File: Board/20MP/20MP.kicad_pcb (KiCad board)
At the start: 2 copper layers, 103.2 x 100 mm, 49 parts, among them J1 Conn_01x02_Male, SW1 SHOU_HAN_MSK12C02-HB, SW2 RotaryEncoder_Switch, U1 nice_nanoV2

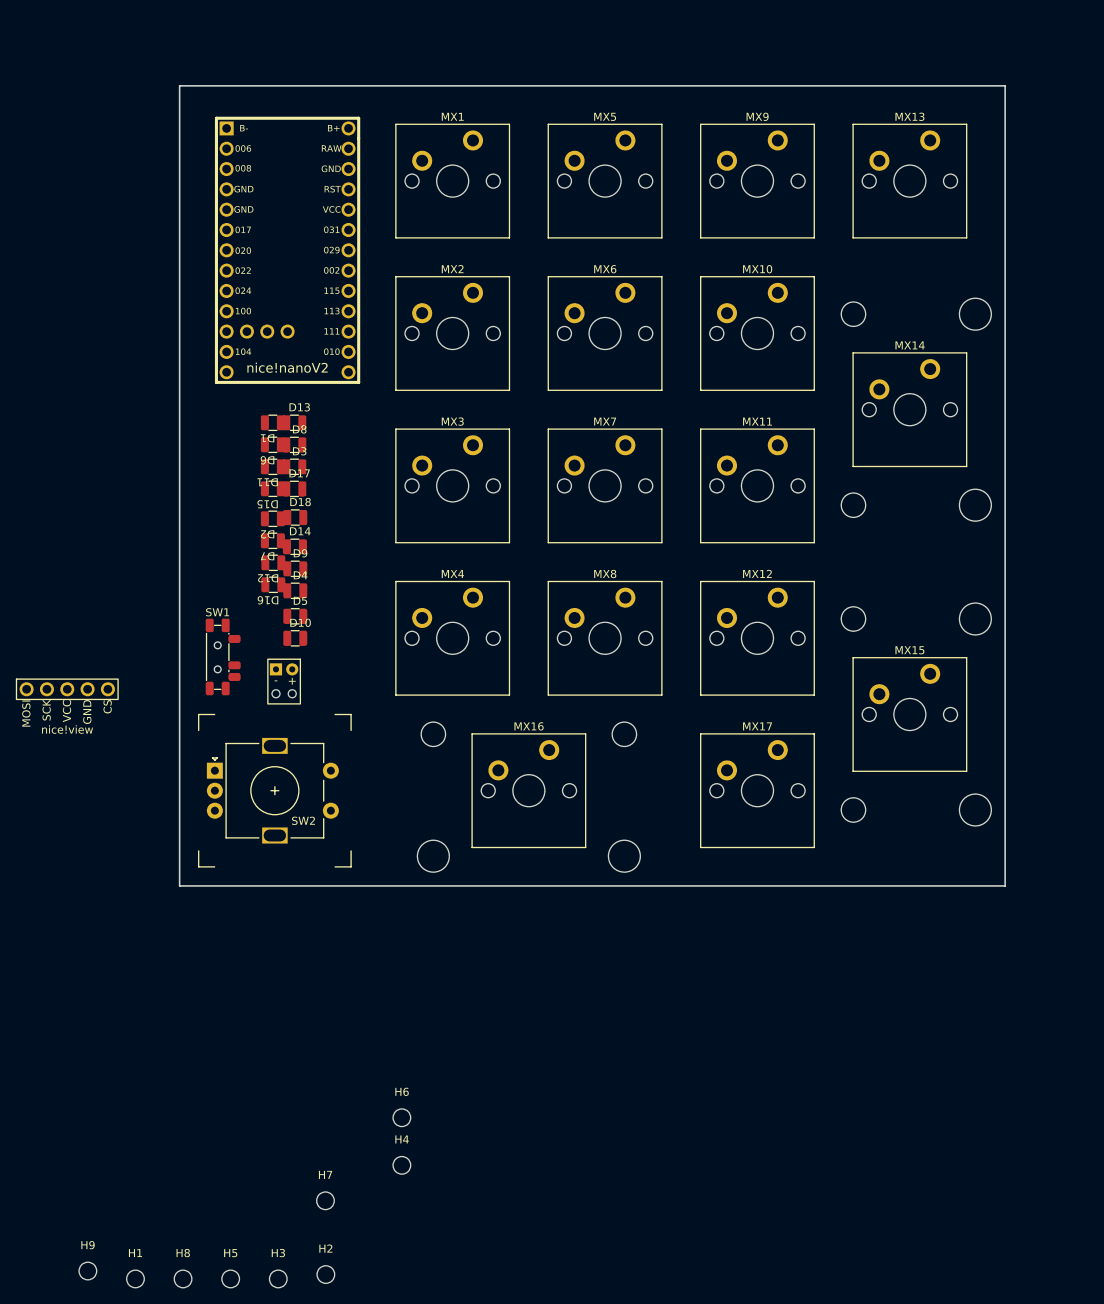
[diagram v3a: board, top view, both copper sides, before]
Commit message: added matrix traces
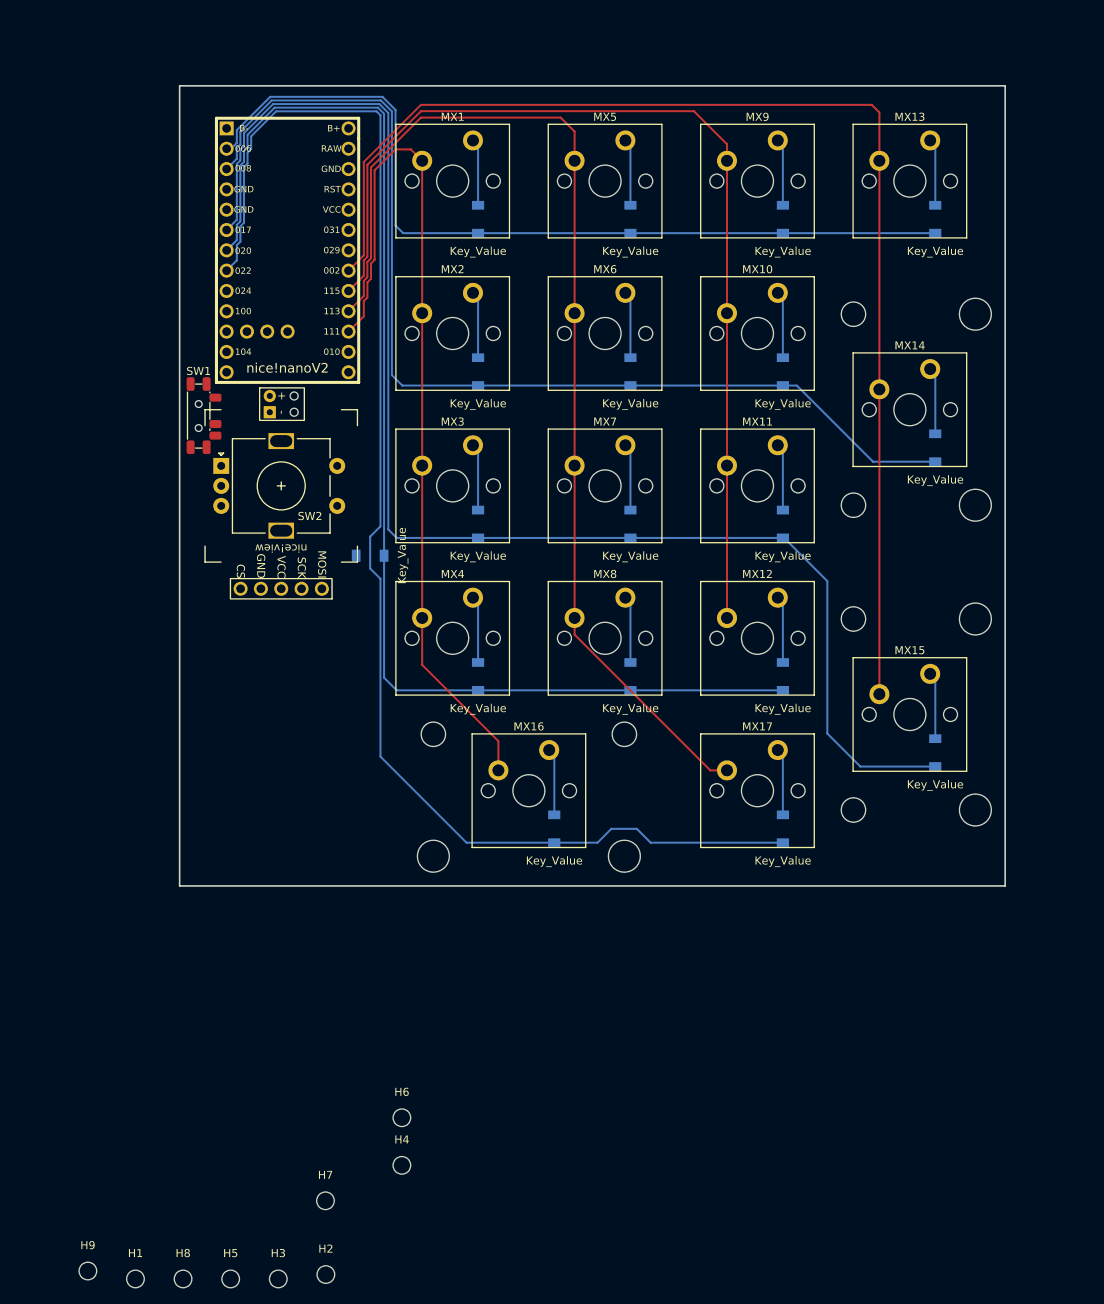
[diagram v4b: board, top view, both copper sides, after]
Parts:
- D1, D10, D11, D12, D13, D14, D15, D16, D17, D18, D2, D3, D4, D5, D6, D7, D8, D9: footprint led:led_capacitor -> led:D_SOD-123; moved to B.Cu
- U1: value nice_nanoV2 -> nice_nano
- moved D15 89.4 mm to (146.1, 50.8), turned to 90 degrees
- moved D17 86.6 mm to (146.1, 117.5), turned to 90 degrees
- moved D16 84.5 mm to (146.1, 79.4), turned to 90 degrees
- moved D11 70.9 mm to (127.0, 50.8), turned to 90 degrees
- moved D12 68.0 mm to (127.0, 69.8), turned to 90 degrees
- moved D10 65.4 mm to (127.0, 127.0), turned to 90 degrees
- moved D14 63.1 mm to (127.0, 108.0), turned to 90 degrees
- moved D13 62.4 mm to (127.0, 88.9), turned to 90 degrees
- moved D6 52.9 mm to (108.0, 50.8), turned to 90 degrees
- moved D7 49.5 mm to (108.0, 69.8), turned to 90 degrees
- moved D9 44.0 mm to (108.0, 108.0), turned to 90 degrees
- moved D8 43.2 mm to (108.0, 88.9), turned to 90 degrees
- moved D5 41.9 mm to (98.4, 127.0), turned to 90 degrees
- moved SW2 38.1 mm to (64.3, 84.1)
- moved D1 36.1 mm to (88.9, 50.8), turned to 90 degrees
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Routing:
- net ROW2: track 0.00 -> 176.9 mm
- net ROW4: track 0.00 -> 173.2 mm
- net ROW3: track 0.00 -> 155.3 mm
- net COL3: track 0.00 -> 154.9 mm
- net COL1: track 0.00 -> 136.9 mm
- net ROW1: track 0.00 -> 131.9 mm
- net COL2: track 0.00 -> 125.4 mm
- net COL0: track 0.00 -> 109.3 mm
- net ROW0: track 0.00 -> 107.7 mm
- net Net-(D17-Pad2): track 0.00 -> 8.36 mm
- net Net-(D16-Pad2): track 0.00 -> 8.36 mm
- net Net-(D15-Pad2): track 0.00 -> 8.36 mm
- net Net-(D10-Pad2): track 0.00 -> 8.36 mm
- net Net-(D7-Pad2): track 0.00 -> 8.36 mm
- net Net-(D6-Pad2): track 0.00 -> 8.36 mm
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
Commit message: added power
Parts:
- moved J1 5.43 mm to (65.4, 75.8), turned to 90 degrees
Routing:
- net B+: track 0.00 -> 57.4 mm, vias 0 -> 2
- net B-: track 0.00 -> 38.1 mm
- net COL3: track 154.9 -> 179.9 mm
- net Net-(J1-Pad2): track 0.00 -> 9.35 mm
- net Net-(D18-Pad2): track 0.00 -> 7.21 mm
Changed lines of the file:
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@@
   )
   (footprint "led:THT_Battery" (layer "F.Cu")
-    (at 61.59475 71.88175 -90)
+    (at 65.40525 75.75575 90)
     (property "Sheetfile" "20MP.kicad_sch")
     (property "Sheetname" "")
     (attr through_hole)
-    (fp_text reference "J1" (at 2.032 -6.604 -90 unlocked) (layer "F.SilkS") hide
-      (effects (font (size 1 1) (thickness 0.15)))
-    )
-    (fp_text value "Conn_01x02_Male" (at 2.187 -6.699 -90 unlocked) (layer "F.Fab")
-      (effects (font (size 1 1) (thickness 0.15)))
-    )
-    (fp_text user "-" (at 3.048 -2.794 -90 unlocked) (layer "F.SilkS")
-      (effects (font (size 1 1) (thickness 0.15)))
-    )
-    (fp_text user "+" (at 1.016 -2.794 -90 unlocked) (layer "F.SilkS")
+    (fp_text reference "J1" (at 2.032 -6.604 90 unlocked) (layer "F.SilkS") hide
+      (effects (font (size 1 1) (thickness 0.15)))
+    )
+    (fp_text value "Conn_01x02_Male" (at 2.187 -6.699 90 unlocked) (layer "F.Fab")
+      (effects (font (size 1 1) (thickness 0.15)))
+    )
+    (fp_text user "-" (at 3.048 -2.794 90 unlocked) (layer "F.SilkS")
+      (effects (font (size 1 1) (thickness 0.15)))
+    )
+    (fp_text user "+" (at 1.016 -2.794 90 unlocked) (layer "F.SilkS")
       (effects (font (size 1 1) (thickness 0.15)))
     )
     (fp_rect (start 0 0) (end 4.064 -5.588) (layer "F.SilkS") (width 0.12) (fill none))
-    (pad "" np_thru_hole circle (at 3.048 -4.318 270) (size 0.001 0.001) (drill 1) (layers F&B.Cu *.Mask))
-    (pad "" np_thru_hole circle (at 1.016 -4.318 270) (size 0.001 0.001) (drill 1) (layers F&B.Cu *.Mask))
-    (pad "1" thru_hole rect (at 3.048 -1.27 270) (size 1.524 1.524) (drill 0.762) (layers *.Cu *.Mask)
+    (pad "" np_thru_hole circle (at 3.048 -4.318 90) (size 0.001 0.001) (drill 1) (layers F&B.Cu *.Mask))
+    (pad "" np_thru_hole circle (at 1.016 -4.318 90) (size 0.001 0.001) (drill 1) (layers F&B.Cu *.Mask))
+    (pad "1" thru_hole rect (at 3.048 -1.27 90) (size 1.524 1.524) (drill 0.762) (layers *.Cu *.Mask)
       (net 24 "B-") (pinfunction "Pin_1") (pintype "passive"))
-    (pad "2" thru_hole circle (at 1.016 -1.27 270) (size 1.524 1.524) (drill 0.762) (layers *.Cu *.Mask)
+    (pad "2" thru_hole circle (at 1.016 -1.27 90) (size 1.524 1.524) (drill 0.762) (layers *.Cu *.Mask)
       (net 25 "Net-(J1-Pad2)") (pinfunction "Pin_2") (pintype "passive"))
   )
@@
   (segment (start 146.05 108.2675) (end 145.415 107.6325) (width 0.25) (layer "B.Cu") (net 22))
   (segment (start 146.05 115.732) (end 146.05 108.2675) (width 0.25) (layer "B.Cu") (net 22))
+  (segment (start 71.29375 86.6375) (end 71.29375 90.49925) (width 0.25) (layer "B.Cu") (net 23))
+  (segment (start 71.29375 90.49925) (end 73.66325 92.86875) (width 0.25) (layer "B.Cu") (net 23))
+  (segment (start 64.13525 72.70775) (end 64.13525 68.421) (width 0.508) (layer "F.Cu") (net 24))
+  (segment (start 59.53125 56.35625) (end 59.53125 41.5155) (width 0.508) (layer "F.Cu") (net 24))
+  (segment (start 66.675 65.88125) (end 66.675 63.5) (width 0.508) (layer "F.Cu") (net 24))
+  (segment (start 59.53125 41.5155) (end 57.4675 39.45175) (width 0.508) (layer "F.Cu") (net 24))
+  (segment (start 64.13525 68.421) (end 66.675 65.88125) (width 0.508) (layer "F.Cu") (net 24))
+  (segment (start 66.675 63.5) (end 59.53125 56.35625) (width 0.508) (layer "F.Cu") (net 24))
+  (segment (start 59.53125 76.2) (end 57.875 77.85625) (width 0.508) (layer "F.Cu") (net 25))
+  (segment (start 64.13525 74.73975) (end 62.675 76.2) (width 0.508) (layer "F.Cu") (net 25))
+  (segment (start 62.675 76.2) (end 59.53125 76.2) (width 0.508) (layer "F.Cu") (net 25))
+  (segment (start 57.875 77.85625) (end 56.075 77.85625) (width 0.508) (layer "F.Cu") (net 25))
   (segment (start 75.0625 60.593146) (end 74.6125 61.043146) (width 0.25) (layer "F.Cu") (net 26))
   (segment (start 74.6125 61.043146) (end 74.6125 62.94675) (width 0.25) (layer "F.Cu") (net 26))
@@
   (segment (start 81.75625 36.5125) (end 74.6125 43.65625) (width 0.25) (layer "F.Cu") (net 29))
   (segment (start 139.065 37.465) (end 138.1125 36.5125) (width 0.25) (layer "F.Cu") (net 29))
+  (segment (start 71.29375 58.6455) (end 72.7075 57.23175) (width 0.25) (layer "B.Cu") (net 29))
+  (segment (start 71.29375 81.6375) (end 71.29375 58.6455) (width 0.25) (layer "B.Cu") (net 29))
+  (segment (start 61.731378 70.64375) (end 56.075 76.300128) (width 0.508) (layer "F.Cu") (net 31))
+  (segment (start 60.325 56.148736) (end 61.222507 57.046243) (width 0.508) (layer "F.Cu") (net 31))
+  (segment (start 61.222507 57.046243) (end 67.46875 63.292486) (width 0.508) (layer "F.Cu") (net 31))
+  (segment (start 66.778757 66.778757) (end 65.88125 67.676264) (width 0.508) (layer "F.Cu") (net 31))
+  (segment (start 67.46875 63.292486) (end 67.46875 65.0875) (width 0.508) (layer "F.Cu") (net 31))
+  (segment (start 60.325 41.275) (end 60.325 43.65625) (width 0.508) (layer "F.Cu") (net 31))
+  (segment (start 61.9125 39.6875) (end 60.325 41.275) (width 0.508) (layer "F.Cu") (net 31))
+  (segment (start 67.46875 66.088764) (end 66.778757 66.778757) (width 0.508) (layer "F.Cu") (net 31))
+  (segment (start 61.9125 70.64375) (end 61.731378 70.64375) (width 0.508) (layer "F.Cu") (net 31))
+  (segment (start 72.7075 39.45175) (end 62.14825 39.45175) (width 0.508) (layer "F.Cu") (net 31))
+  (segment (start 56.075 76.300128) (end 56.075 76.40625) (width 0.508) (layer "F.Cu") (net 31))
+  (segment (start 62.14825 39.45175) (end 61.9125 39.6875) (width 0.508) (layer "F.Cu") (net 31))
+  (segment (start 65.88125 67.676264) (end 65.88125 69.05625) (width 0.508) (layer "F.Cu") (net 31))
+  (segment (start 60.325 43.65625) (end 60.325 56.148736) (width 0.508) (layer "F.Cu") (net 31))
+  (segment (start 67.46875 65.0875) (end 67.46875 66.088764) (width 0.508) (layer "F.Cu") (net 31))
+  (via (at 61.9125 70.64375) (size 1.016) (drill 0.4) (layers "F.Cu" "B.Cu") (net 31))
+  (via (at 65.88125 69.05625) (size 1.016) (drill 0.4) (layers "F.Cu" "B.Cu") (net 31))
+  (segment (start 65.88125 69.05625) (end 65.0875 69.85) (width 0.508) (layer "B.Cu") (net 31))
+  (segment (start 65.0875 69.85) (end 62.70625 69.85) (width 0.508) (layer "B.Cu") (net 31))
+  (segment (start 62.70625 69.85) (end 61.9125 70.64375) (width 0.508) (layer "B.Cu") (net 31))
 )

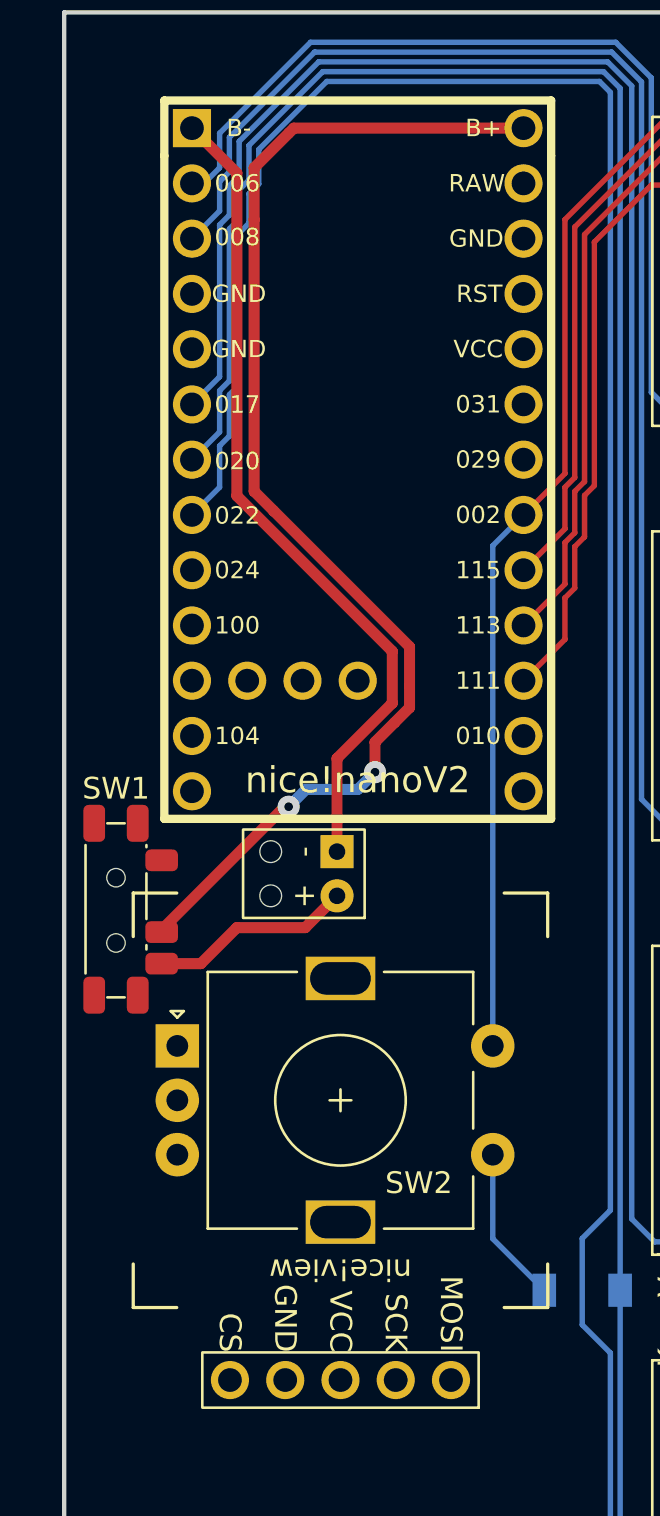
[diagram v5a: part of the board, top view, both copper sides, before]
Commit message: wired oled on pcb
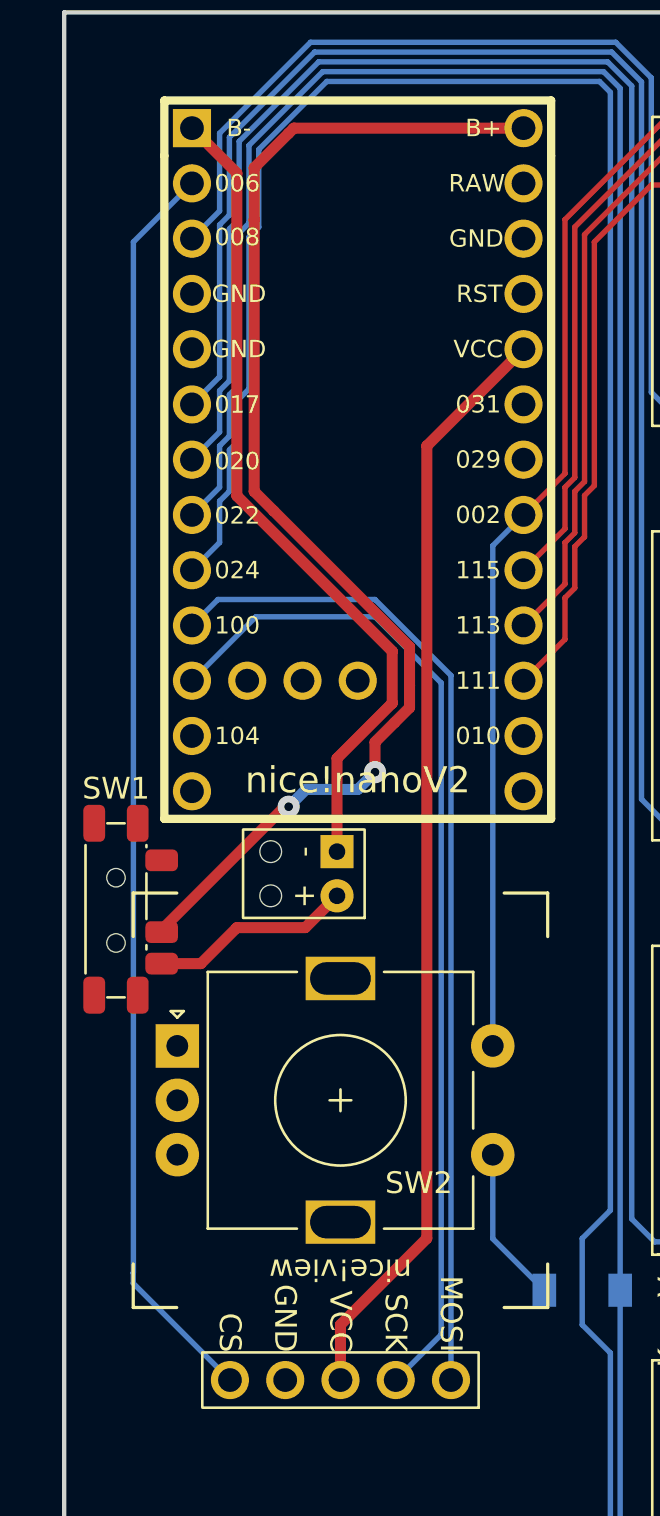
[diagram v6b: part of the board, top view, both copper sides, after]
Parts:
- U1: value nice_nano -> nice_nanoV2
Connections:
- U1 pad 10: SCK -> MOSI
- U1 pad 11: CS -> SCK
- U1 pad 16: COL0 -> unconnected-(U1-Pad16)
- U1 pad 17: COL1 -> COL0
- U1 pad 18: COL2 -> COL1
- U1 pad 19: COL3 -> COL2
- U1 pad 2: ROW0 -> CS
- U1 pad 20: COL4 -> COL3
- U1 pad 21: unconnected-(U1-Pad21) -> COL4
- U1 pad 3: ROW1 -> ROW0
- U1 pad 6: ROW2 -> ROW1
- U1 pad 7: ROW3 -> ROW2
- U1 pad 8: ROW4 -> ROW3
- U1 pad 9: MOSI -> ROW4
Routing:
- net CS: track 0.00 -> 58.5 mm
- net VCC: track 0.00 -> 50.9 mm
- net SCK: track 0.00 -> 46.8 mm
- net MOSI: track 0.00 -> 46.2 mm
- net ROW1: track 131.9 -> 139.5 mm
- net ROW4: track 173.2 -> 175.7 mm
- net ROW3: track 155.3 -> 157.8 mm
- net ROW2: track 176.9 -> 179.4 mm
- net ROW0: track 107.7 -> 109.9 mm

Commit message: finished pcb
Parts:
- moved H7 159.1 mm to (150.8, 36.5)
- moved H2 147.1 mm to (54.0, 36.5)
- moved H9 130.2 mm to (95.2, 64.3)
- moved H1 86.0 mm to (95.2, 112.7)
- moved H6 78.7 mm to (150.8, 130.2)
- moved H4 46.5 mm to (54.0, 130.2)
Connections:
- SW2 pad S2: COL3 -> COL2
- U1 pad 15: unconnected-(U1-Pad15) -> /ROT_1A
- U1 pad 16: unconnected-(U1-Pad16) -> /ROT_1B
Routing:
- net /ROT_1B: track 0.00 -> 32.3 mm, vias 0 -> 1
- net COL3: track 179.9 -> 152.3 mm
- net /ROT_1A: track 0.00 -> 26.1 mm, vias 0 -> 1
- net COL2: track 125.4 -> 147.8 mm
- net COL1: track 136.9 -> 134.3 mm
- net COL0: track 109.3 -> 106.7 mm
- net SCK: track 46.8 -> 45.1 mm
- added copper zone on B.Cu, net GND
- added copper zone on F.Cu, net GND
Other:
- board size 103.2 x 100 mm -> 104.8 x 101.6 mm
